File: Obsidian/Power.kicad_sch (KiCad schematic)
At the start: 80 parts, among them J10 Barrel_Jack_Switch, J16 Conn_01x04, Q4 DMP3013SFV, U10 TPSM863257RDXR, U11 TPSM863257RDXR, U18 TLV77325PDBVR, U20 RT9045AGSP / AP2303, U23 LD39100PU12RY, U24 SN74LVC1G07DBV, U25 SN74LVC1G07DBV, U4 TPSM863257RDXR, U5 TPSM863257RDXR, U6 TPSM863257RDXR

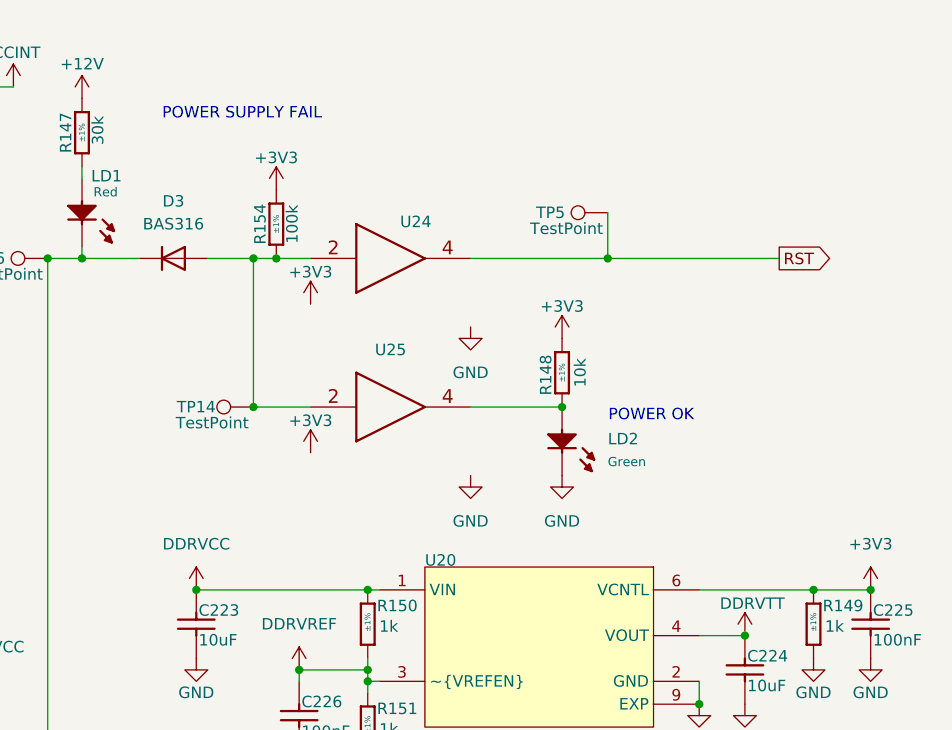
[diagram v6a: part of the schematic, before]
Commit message: correct SN74LVC1G07DBV floating pins
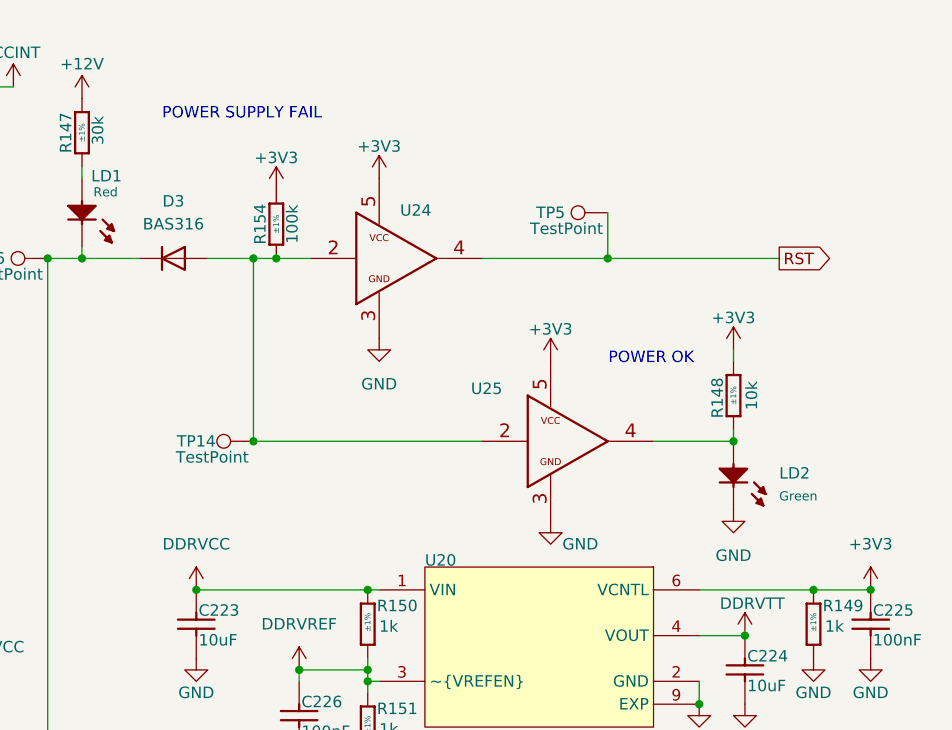
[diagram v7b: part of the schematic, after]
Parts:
- U24: footprint Footprint:SOT95P280X145-5N -> ICs And Semiconductors SMD:SOT95P280X145-5N
- U25: footprint Footprint:SOT95P280X145-5N -> ICs And Semiconductors SMD:SOT95P280X145-5N; symbol Library_Symbol:SN74LVC1G07DBV -> Library_Symbol:SN74LVC1G07DBV_1
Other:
- moved on the sheet: LD2, R148, TP14

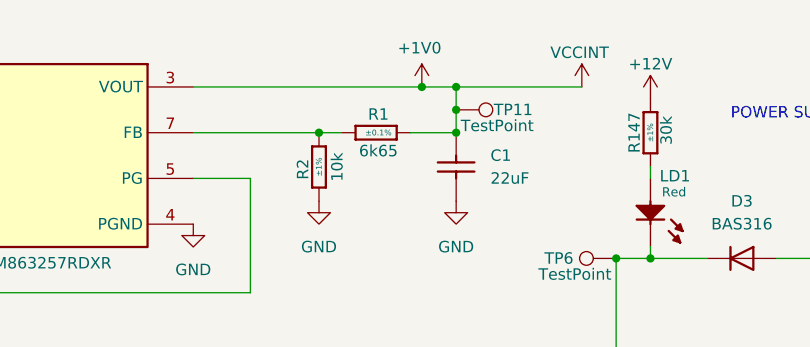
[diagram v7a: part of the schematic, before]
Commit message: deleting two labels on 1V net, replacing with VCCINT_1V
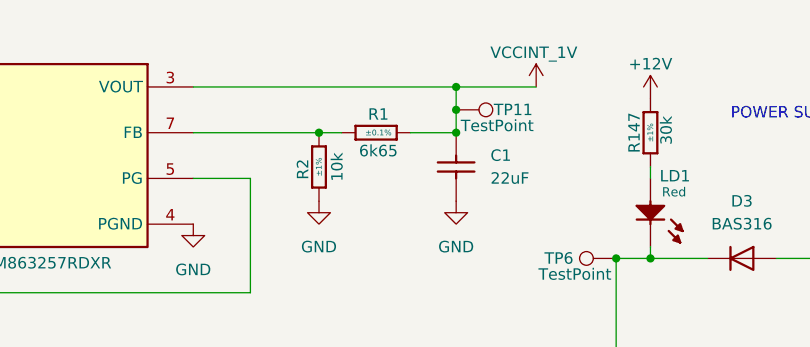
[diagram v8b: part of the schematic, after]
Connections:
- net +1V0 renamed VCCINT_1V
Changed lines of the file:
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@@
 	)
 	(junction
-		(at 151.13 17.78)
-		(diameter 0)
-		(color 0 0 0 0)
-	)
-	(junction
 		(at 90.17 62.23)
 		(diameter 0)
@@
 	(wire
 		(pts
-			(xy 154.94 17.78) (xy 168.91 17.78)
+			(xy 154.94 17.78) (xy 163.83 17.78)
 		)
 		(stroke
@@
 	(wire
 		(pts
-			(xy 151.13 17.78) (xy 154.94 17.78)
-		)
-		(stroke
-			(width 0)
-			(type default)
-		)
-	)
-	(wire
-		(pts
 			(xy 92.71 129.54) (xy 92.71 127)
 		)
@@
 	(wire
 		(pts
-			(xy 125.73 17.78) (xy 151.13 17.78)
+			(xy 125.73 17.78) (xy 154.94 17.78)
 		)
 		(stroke
@@
 	(symbol
 		(lib_id "Library_Symbol:+1V0")
-		(at 168.91 17.78 0)
+		(at 163.83 17.78 0)
 		(unit 1)
 		(exclude_from_sim no)
@@
 		(dnp no)
 		(property "Reference" "#PWR0184"
-			(at 168.91 21.59 0)
+			(at 163.83 21.59 0)
 			(effects
 				(font
@@
 			)
 		)
-		(property "Value" "VCCINT"
-			(at 168.656 13.97 0)
+		(property "Value" "VCCINT_1V"
+			(at 163.576 13.97 0)
 			(effects
 				(font
@@
 		)
 		(property "Footprint" ""
-			(at 168.91 17.78 0)
+			(at 163.83 17.78 0)
 			(effects
 				(font
@@
 		)
 		(property "Datasheet" ""
-			(at 168.91 17.78 0)
+			(at 163.83 17.78 0)
 			(effects
 				(font
@@
 		)
 		(property "Description" "Power symbol creates a global label with name \"+1V0\""
-			(at 168.91 17.78 0)
+			(at 163.83 17.78 0)
 			(effects
 				(font
@@
 					(unit 1)
 				)
-			)
-		)
-	)
-	(symbol
-		(lib_id "Library_Symbol:+1V0")
-		(at 151.13 17.78 0)
-		(unit 1)
-		(exclude_from_sim no)
-		(in_bom yes)
-		(on_board yes)
-		(dnp no)
-		(property "Reference" "#PWR02"
-			(at 151.13 21.59 0)
-			(effects
-				(font
-					(size 1.27 1.27)
-				)
-				(hide yes)
-			)
-		)
-		(property "Value" "+1V0"
-			(at 150.876 13.462 0)
-			(effects
-				(font
-					(size 1.27 1.27)
-				)
-			)
-		)
-		(property "Footprint" ""
-			(at 151.13 17.78 0)
-			(effects
-				(font
-					(size 1.27 1.27)
-				)
-				(hide yes)
-			)
-		)
-		(property "Datasheet" ""
-			(at 151.13 17.78 0)
-			(effects
-				(font
-					(size 1.27 1.27)
-				)
-				(hide yes)
-			)
-		)
-		(property "Description" "Power symbol creates a global label with name \"+1V0\""
-			(at 151.13 17.78 0)
-			(effects
-				(font
-					(size 1.27 1.27)
-				)
-				(hide yes)
-			)
-		)
-		(pin "1"
-		)
-		(instances
-			(project ""
-				(path "/c2a4f786-b14c-434a-acf7-b20fb2221b0b/1f98e56a-3346-4f12-a356-5cd64c4ccde0"
-					(reference "#PWR02")
-					(unit 1)
-				)
